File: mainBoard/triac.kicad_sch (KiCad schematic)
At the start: 18 parts, among them J4 Conn_01x03, J5 1366005, U2 DS18B20+, U3 MOC3083S-TA1

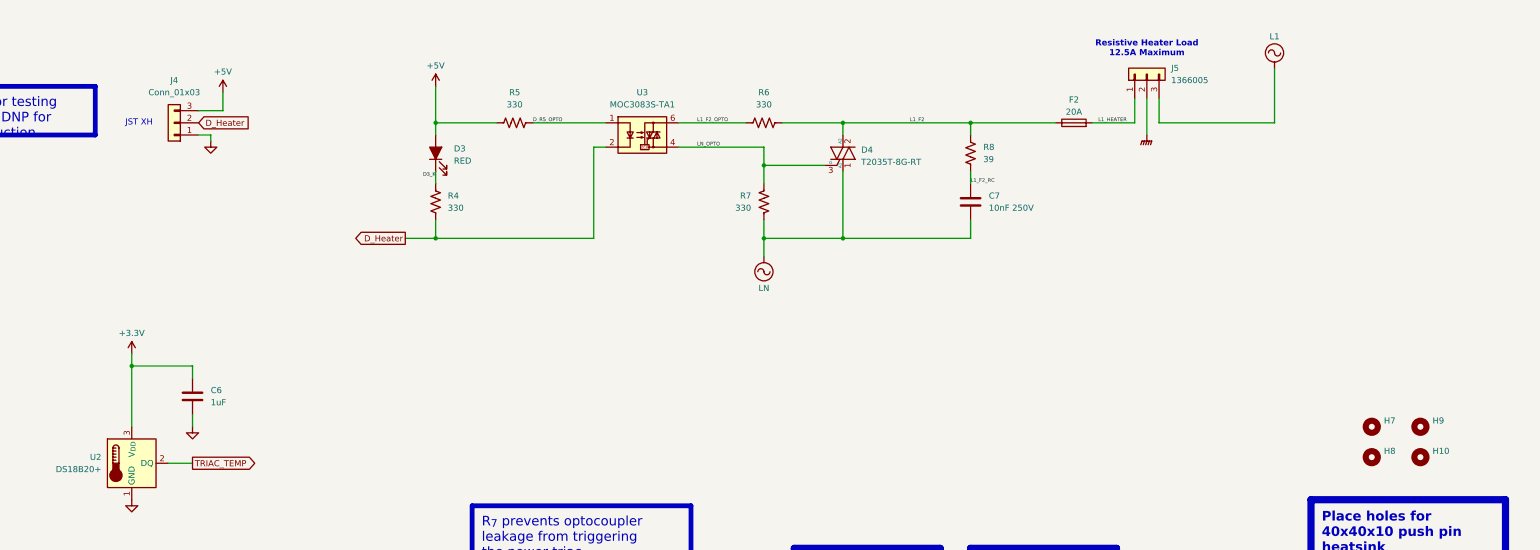
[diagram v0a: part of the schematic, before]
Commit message: Schematic Capture should be complete, ready for PCB
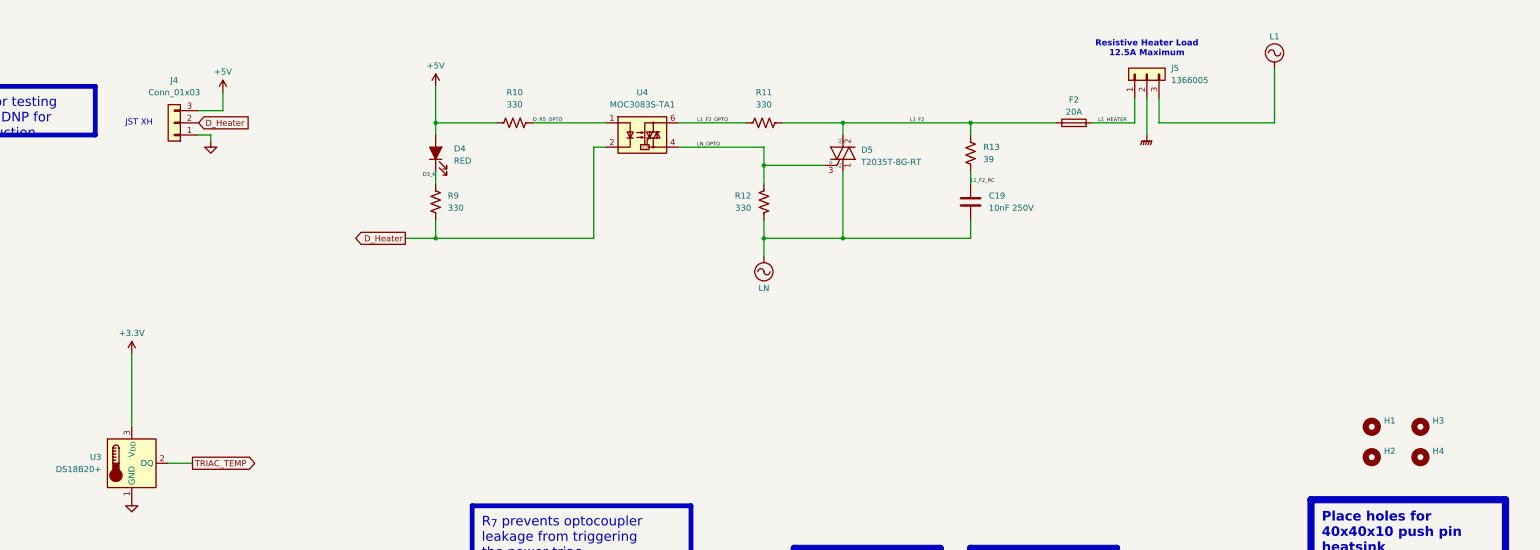
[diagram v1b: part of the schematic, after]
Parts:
- removed C6: 1uF, Capacitor_SMD:C_0805_2012Metric_Pad1.18x1.45mm_HandSolder, symbol Device:C
- renumbered C7 to C19, D3 to D4, D4 to D5, H7 to H1, H8 to H2, H9 to H3, H10 to H4, R5 to R10, R6 to R11, R7 to R12, R8 to R13, R4 to R9, U2 to U3, U3 to U4

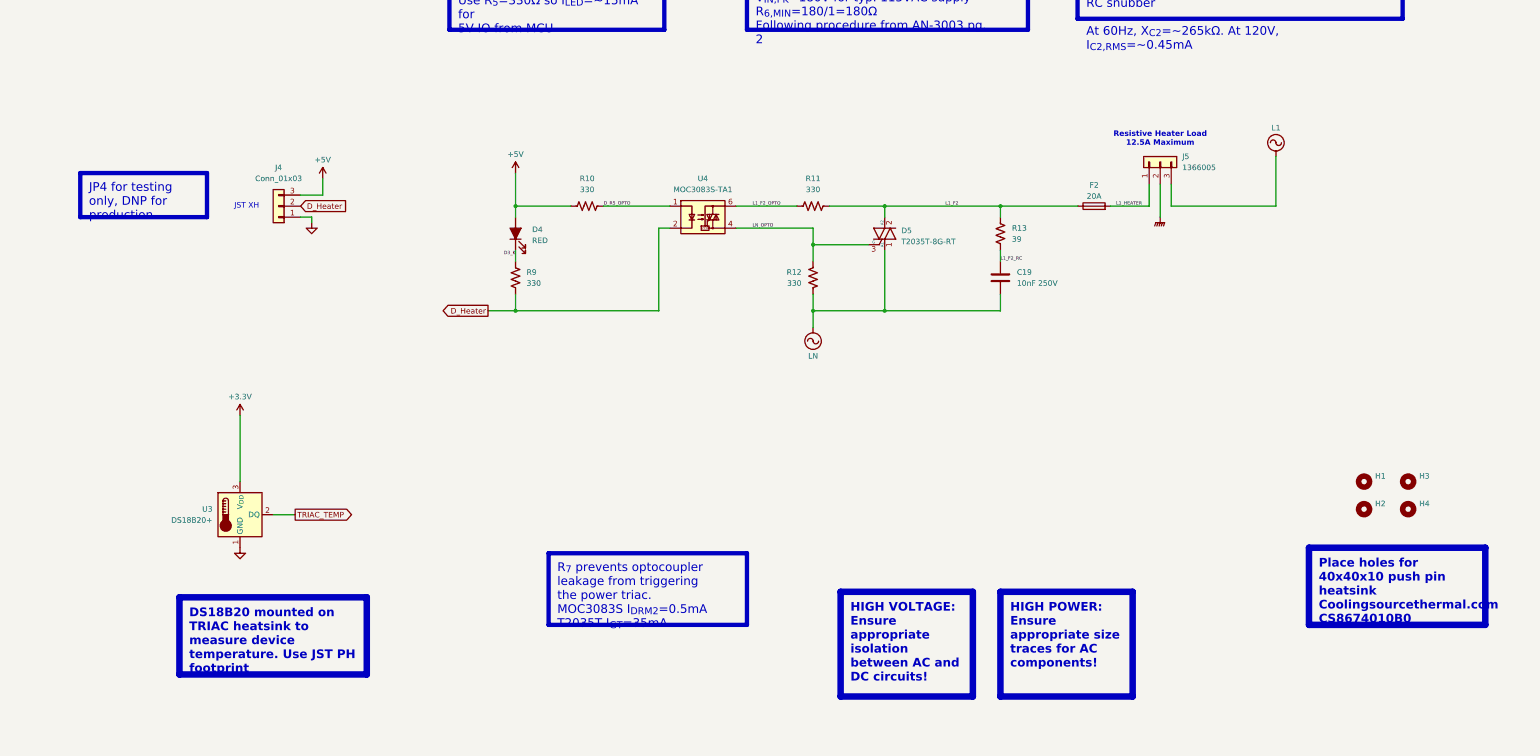
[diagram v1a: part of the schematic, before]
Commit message: tweak schematic for changes from 6-17-2026
major structural changes, see daily note from obsidian
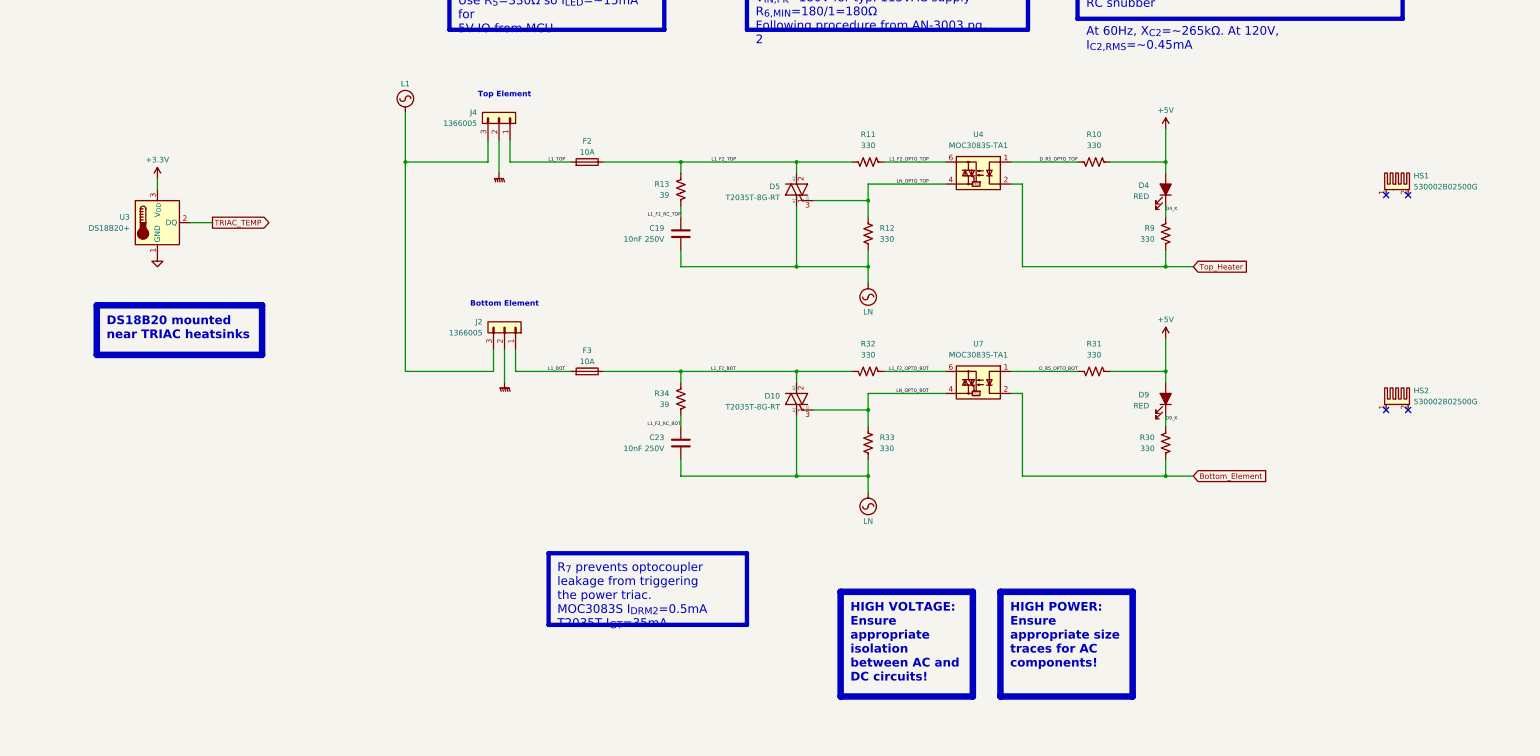
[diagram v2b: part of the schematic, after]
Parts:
- removed H1, H2, H3, H4: MountingHole, MountingHole:MountingHole_3mm, symbol Mechanical:MountingHole
- removed J4: Conn_01x03, Connector_JST:JST_XH_B3B-XH-A_1x03_P2.50mm_Vertical, symbol Connector_Generic:Conn_01x03
- added C23: 10nF 250V, Capacitor_SMD:C_1812_4532Metric_Pad1.57x3.40mm_HandSolder, symbol Device:C
- added D10: T2035T-8G-RT, Package_TO_SOT_THT:TO-220-3_Vertical, symbol Triac_Thyristor:Generic_Triac_A1A2G
- added D9: RED, LED_SMD:LED_0603_1608Metric_Pad1.05x0.95mm_HandSolder, symbol Device:LED_Filled
- added F3: 10A, Fuse:Fuseholder_Clip-6.3x32mm_Littelfuse_122_Inline_P34.21x7.62mm_D2.54mm_Horizontal, symbol Device:Fuse
- added HS1, HS2: 530002B02500G, 530002_Heatsinks:53002B02500G, symbol Mechanical:Heatsink_Pad_2Pin
- added J2: 1366005, PhoenixContact_SPTA:SPTA-THR 2.53-5.0 P26, symbol Connector_Generic:Conn_01x03
- added R30, R31: 330, Resistor_SMD:R_0603_1608Metric_Pad0.98x0.95mm_HandSolder, symbol Device:R_US
- added R32, R33: 330, Resistor_SMD:R_2512_6332Metric_Pad1.40x3.35mm_HandSolder, symbol Device:R_US
- added R34: 39, Resistor_SMD:R_2512_6332Metric_Pad1.40x3.35mm_HandSolder, symbol Device:R_US
- added U7: MOC3083S-TA1, Package_DIP:SMDIP-6_W9.53mm, symbol Relay_SolidState:MOC3083M
- D5: footprint Package_TO_SOT_SMD:TO-263-2 -> Package_TO_SOT_THT:TO-220-3_Vertical
- F2: value 20A -> 10A
- U3: footprint Connector_JST:JST_PH_B3B-PH-K_1x03_P2.00mm_Vertical -> Package_TO_SOT_THT:TO-92_Inline
- renumbered J5 to J4
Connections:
- net +5V: now also D9.2 (A), R31.1
- net GNDPWR: now also J2.2 (Pin_2)
- net L1: now also J2.3 (Pin_3)
- net LN: now also C23.2, D10.1 (A1), R33.1
- net D3_K renamed D4_K
- net D_Heater renamed Top_Heater
- net D_R5_OPTO renamed D_R5_OPTO_TOP
- net L1_F2 renamed L1_F2_TOP
- net L1_F2_OPTO renamed L1_F2_OPTO_TOP
- net L1_F2_RC renamed L1_F2_RC_TOP
- net L1_HEATER renamed L1_TOP
- net LN_OPTO renamed LN_OPTO_TOP
- new net Bottom_Element: R30.2, U7.2
- new net D9_K: D9.1 (K), R30.1
- new net D_R5_OPTO_BOT: R31.2, U7.1
- new net L1_BOT: F3.2, J2.1 (Pin_1)
- new net L1_F2_BOT: D10.2 (A2), F3.1, R32.2, R34.2
- new net L1_F2_OPTO_BOT: R32.1, U7.6
- new net L1_F2_RC_BOT: C23.1, R34.1
- new net LN_OPTO_BOT: D10.3 (G), R33.2, U7.4
- no-connect marks 0 -> 4
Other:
- note added: "Bottom Element"
- note added: "Top Element"
- note removed: "JST XH"
- note removed: "Resistive Heater Load 12.5A Maximum"
- moved on the sheet: C19, D4, D5, F2, J4, R10, R11, R12, R13, R9, U3, U4

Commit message: working on pcb layout after bringing in work from laptop
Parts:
- removed R30, R31: 330, Resistor_SMD:R_0603_1608Metric_Pad0.98x0.95mm_HandSolder, symbol Device:R_US
- removed U3: DS18B20+, Package_TO_SOT_THT:TO-92_Inline, symbol Sensor_Temperature:DS18B20
- added Q1, Q2: IRLML6244TRPBF, Package_TO_SOT_SMD:SOT-23, symbol Transistor_FET:IRLML6244
- added R18, R19: 220, Resistor_SMD:R_0603_1608Metric_Pad0.98x0.95mm_HandSolder, symbol Device:R_US
- added R21, R25: 330, Resistor_SMD:R_0603_1608Metric_Pad0.98x0.95mm_HandSolder, symbol Device:R_US
- added R22, R23: 10k, Resistor_SMD:R_0603_1608Metric_Pad0.98x0.95mm_HandSolder, symbol Device:R_US
- added U14, U15: DS18B20+, Connector_JST:JST_XH_B3B-XH-A_1x03_P2.50mm_Vertical, symbol Sensor_Temperature:DS18B20
- renumbered C19 to C25, C23 to C26, D5 to D6, D10 to D7, D4 to D8, J4 to J2, J2 to J3, R13 to R12, R34 to R13, R11 to R14, R12 to R15, R32 to R16, R33 to R17, R10 to R20, R9 to R24, U4 to U6
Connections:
- net +3.3V: now also U14.3 (V_{DD}), U15.3 (V_{DD})
- net +5V: now also R21.1
- net D9_K: now also R25.1
- net GND: now also Q1.2 (S), Q2.2 (S), R22.2, R23.2, U14.1 (GND), U15.1 (GND)
- net Top_Heater: now also R18.1; no longer R24.2, U6.2
- net Bottom_Element renamed OPTO_K_BOT
- net OPTO_K_BOT: now also Q2.3 (D), R25.2
- net D_R5_OPTO_BOT renamed OPTO_A_BOT
- net OPTO_A_BOT: now also R21.2
- net D_R5_OPTO_TOP renamed OPTO_A_TOP
- new net Bottom_Heater: R19.1
- new net OPTO_FET_BOT: Q2.1 (G), R19.2, R23.1
- new net OPTO_FET_TOP: Q1.1 (G), R18.2, R22.1
- new net OPTO_K_TOP: Q1.3 (D), R24.2, U6.2
- new net TRIAC_BOT_TEMP: U15.2 (DQ)
- new net TRIAC_TOP_TEMP: U14.2 (DQ)
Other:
- moved on the sheet: C25, C26, D6, D7, D8, F2, F3, HS1, HS2, J2, J3, R12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

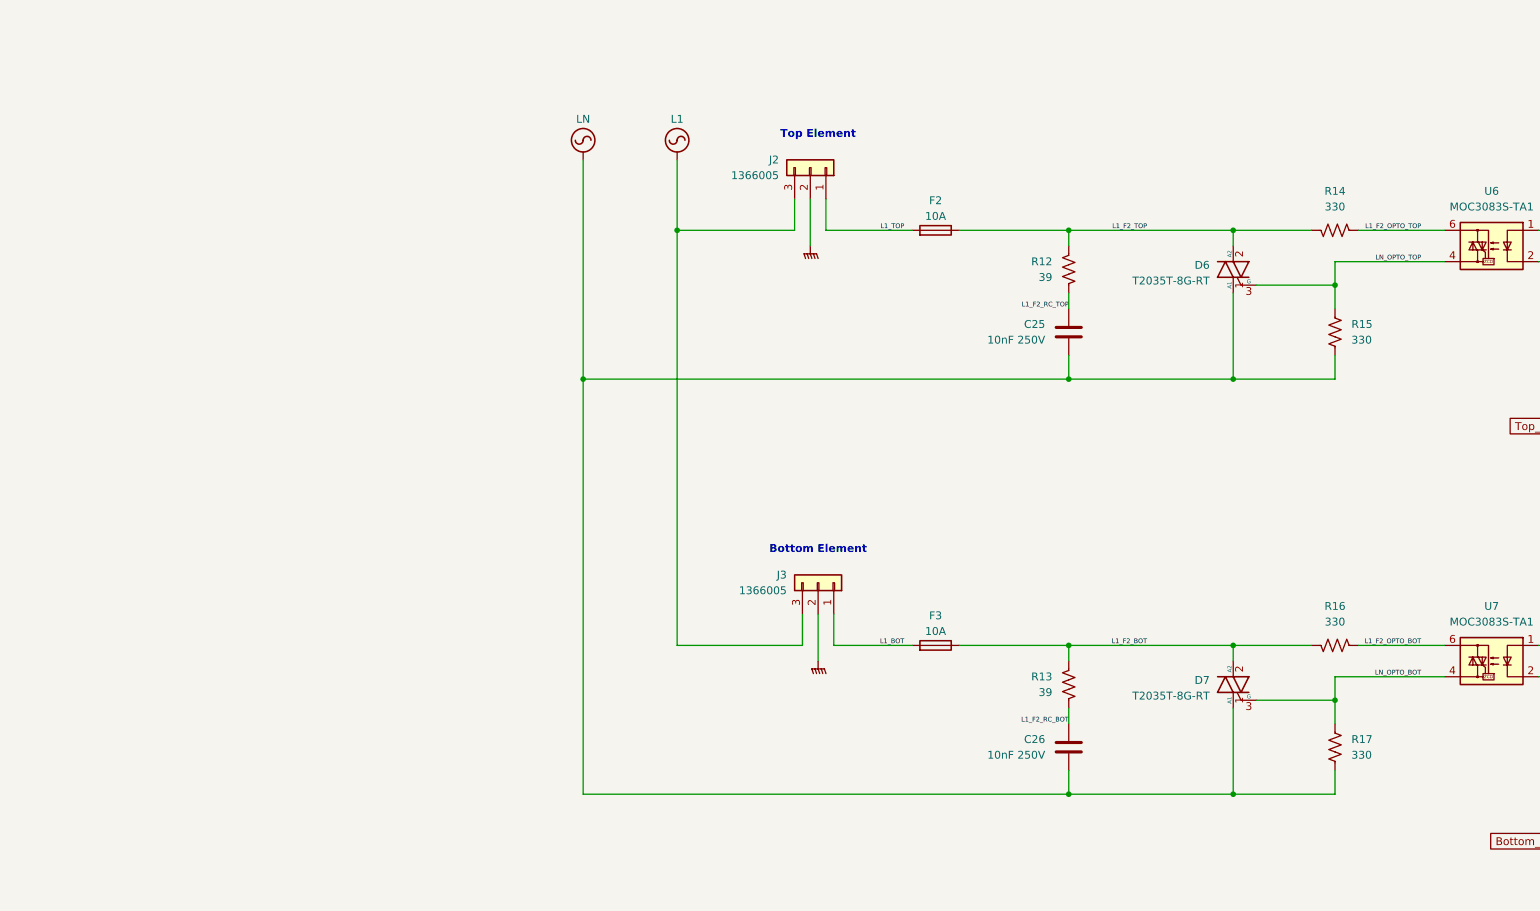
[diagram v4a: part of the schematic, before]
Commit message: reworked AC switching and fusing
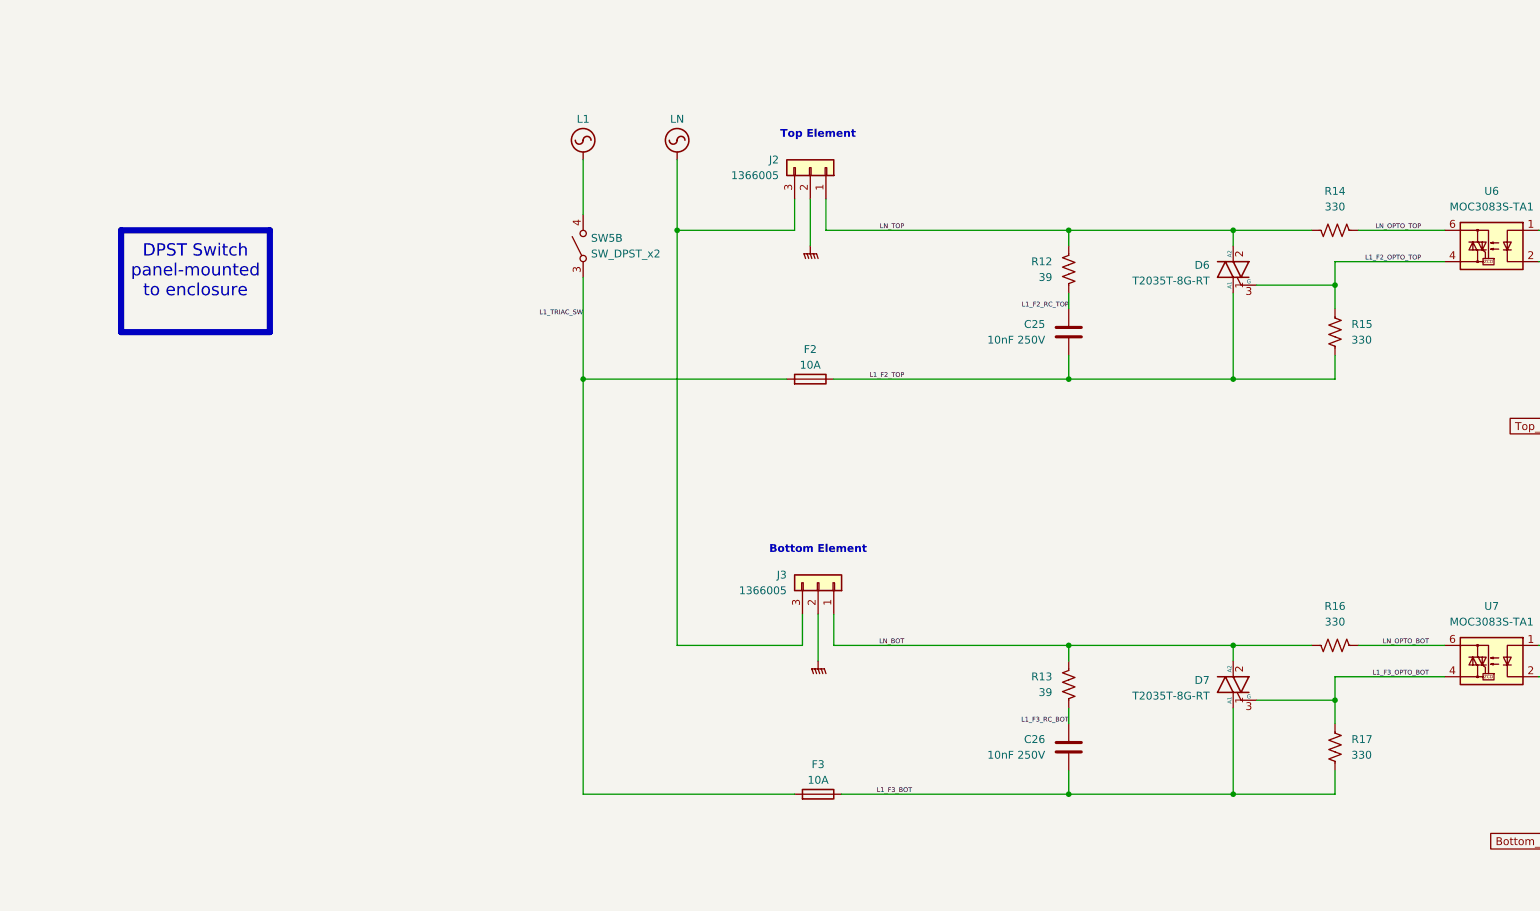
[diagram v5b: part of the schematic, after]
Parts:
- added SW5: SW_DPST_x2, TerminalBlock_Phoenix:TerminalBlock_Phoenix_MKDS-1,5-2-5.08_1x02_P5.08mm_Horizontal, symbol Switch:SW_DPST_x2
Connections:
- net L1_F2_OPTO_BOT is gone; now on net LN_OPTO_BOT: R16.1, U7.6
- net L1: now also SW5.4 (B); no longer J2.3 (Pin_3), J3.3 (Pin_3)
- net L1_F2_OPTO_TOP: now also D6.3 (G), R15.2, U6.4; no longer R14.1, U6.6
- net L1_F2_TOP: now also C25.2, D6.1 (A1), R15.1; no longer D6.2 (A2), R12.2, R14.2
- net LN: now also J2.3 (Pin_3), J3.3 (Pin_3); no longer C25.2, C26.2, D6.1 (A1), D7.1 (A1), R15.1, R17.1
- net LN_OPTO_BOT: no longer D7.3 (G), R17.2, U7.4
- net LN_OPTO_TOP: now also R14.1, U6.6; no longer D6.3 (G), R15.2, U6.4
- net L1_BOT renamed L1_TRIAC_SW
- net L1_TRIAC_SW: now also F2.2, SW5.3 (A); no longer J3.1 (Pin_1)
- net L1_F2_BOT renamed LN_BOT
- net LN_BOT: now also J3.1 (Pin_1); no longer F3.1
- net L1_F2_RC_BOT renamed L1_F3_RC_BOT
- net L1_TOP renamed LN_TOP
- net LN_TOP: now also D6.2 (A2), R12.2, R14.2; no longer F2.2
- new net L1_F3_BOT: C26.2, D7.1 (A1), F3.1, R17.1
- new net L1_F3_OPTO_BOT: D7.3 (G), R17.2, U7.4
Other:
- moved on the sheet: F2, F3

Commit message: Add pullup resistors to digital thermometers
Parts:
- added R69, R70: 4.7k, Resistor_SMD:R_0603_1608Metric_Pad0.98x0.95mm_HandSolder, symbol Device:R_US
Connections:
- net +3.3V: now also R69.1, R70.1
- net TRIAC_BOT_TEMP: now also R69.2
- net TRIAC_TOP_TEMP: now also R70.2
